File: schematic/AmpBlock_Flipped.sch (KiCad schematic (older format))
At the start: 12 parts, among them IC8 LTC6090CS8E#PBF

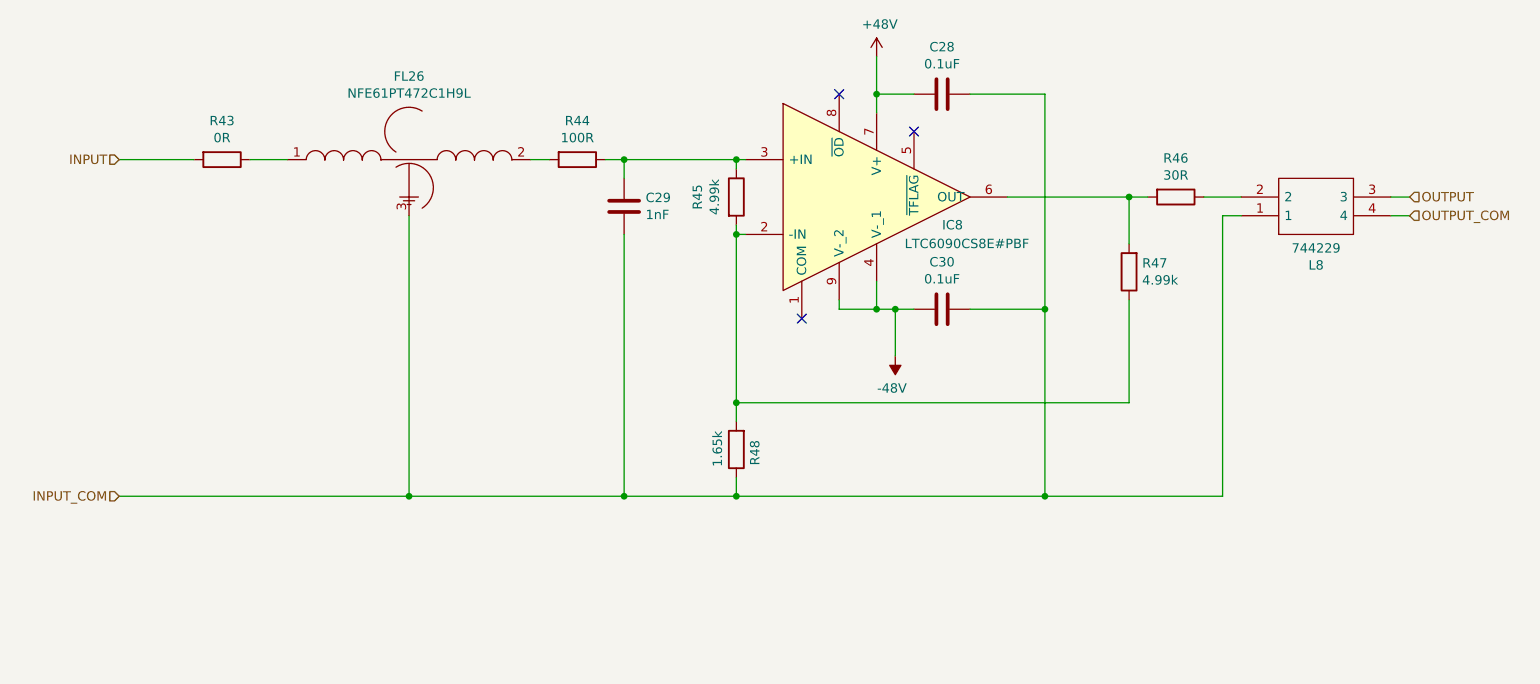
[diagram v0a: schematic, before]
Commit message: Updating with recent changes as layout work starts
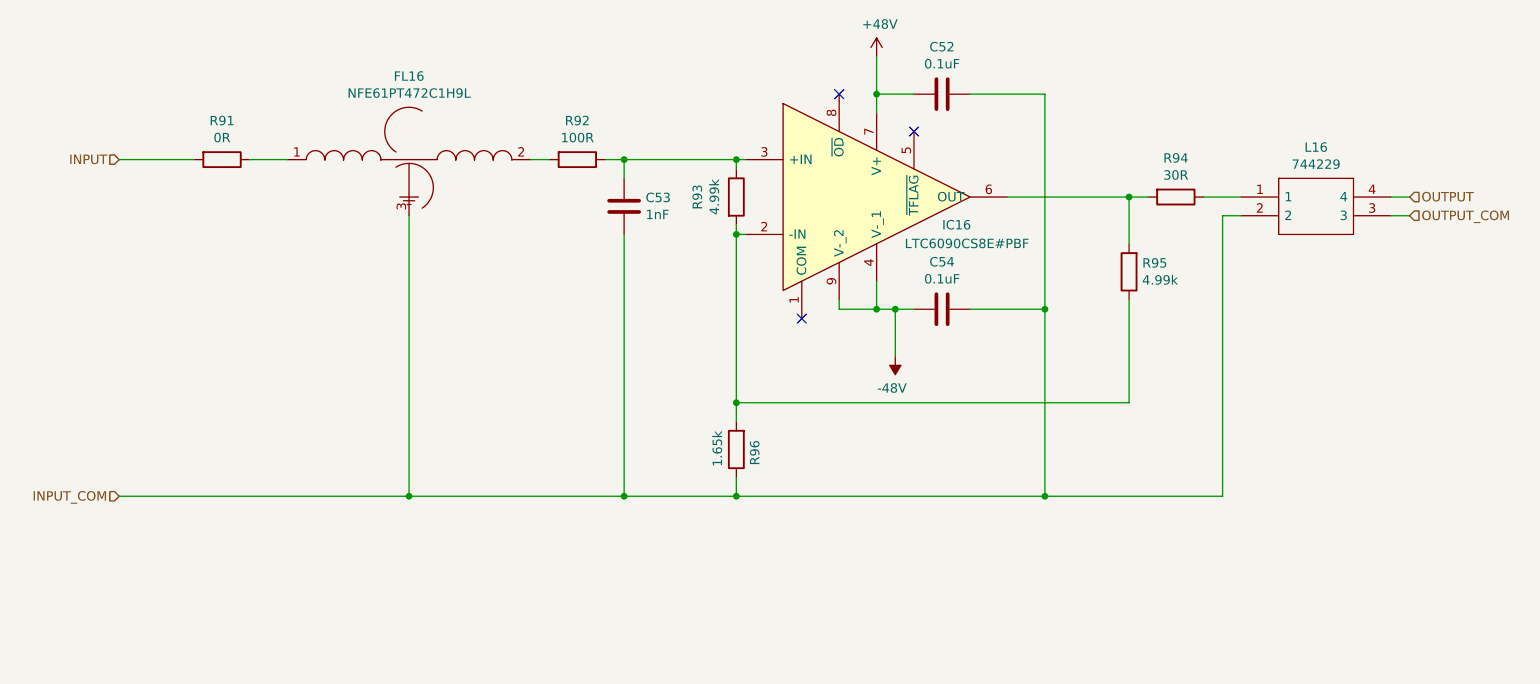
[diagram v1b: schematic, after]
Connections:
- net INPUT_COM: now also L8.2; no longer L8.1
- net OUTPUT: now also L8.4; no longer L8.3
- net OUTPUT_COM: now also L8.3; no longer L8.4
- net at R46.1: now also L8.1; no longer L8.2
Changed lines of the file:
@@
 $Descr A4 11693 8268
 encoding utf-8
-Sheet 26 33
+Sheet 17 33
 Title "Amplifier block"
 Date ""
@@
 AR Path="/5CAE2EB0/5C968DBB" Ref="R188"  Part="1"
 AR Path="/5C968DBB" Ref="R?"  Part="1"
-F 0 "R?" V 3743 3400 50  0000 C CNN
+F 0 "R92" V 3743 3400 50  0000 C CNN
 F 1 "100R" V 3834 3400 50  0000 C CNN
 F 2 "Resistor_SMD:R_0603_1608Metric" V 3880 3400 50  0001 C CNN
@@
 AR Path="/5CAE2EB0/5C969C02" Ref="R192"  Part="1"
 AR Path="/5C969C02" Ref="R?"  Part="1"
-F 0 "R?" V 4700 4900 50  0000 L CNN
+F 0 "R96" V 4700 4900 50  0000 L CNN
 F 1 "1.65k" V 4900 4850 50  0000 L CNN
 F 2 "Resistor_SMD:R_0603_1608Metric" V 4730 4950 50  0001 C CNN
@@
 AR Path="/5CAE2EB0/5C96A29C" Ref="R191"  Part="1"
 AR Path="/5C96A29C" Ref="R?"  Part="1"
-F 0 "R?" H 6830 3954 50  0000 R CNN
+F 0 "R95" H 6830 3954 50  0000 R CNN
 F 1 "4.99k" H 6830 4045 50  0000 R CNN
 F 2 "Resistor_SMD:R_0603_1608Metric" V 6830 4000 50  0001 C CNN
@@
 AR Path="/5CAE2EB0/5C96A628" Ref="C101"  Part="1"
 AR Path="/5C96A628" Ref="C?"  Part="1"
-F 0 "C?" H 4315 3696 50  0000 L CNN
+F 0 "C53" H 4315 3696 50  0000 L CNN
 F 1 "1nF" H 4315 3605 50  0000 L CNN
 F 2 "Capacitor_SMD:C_0603_1608Metric" H 4238 3500 50  0001 C CNN
@@
 AR Path="/5CAE2EB0/5C96EFD0" Ref="#PWR073"  Part="1"
 AR Path="/5C96EFD0" Ref="#PWR?"  Part="1"
-F 0 "#PWR?" H 5550 2700 50  0001 C CNN
+F 0 "#PWR073" H 5550 2700 50  0001 C CNN
 F 1 "+48V" H 5567 3023 50  0000 C CNN
 F 2 "" H 5550 2850 50  0001 C CNN
@@
 AR Path="/5CAE2EB0/5C96F7F1" Ref="#PWR074"  Part="1"
 AR Path="/5C96F7F1" Ref="#PWR?"  Part="1"
-F 0 "#PWR?" H 5650 4300 50  0001 C CNN
+F 0 "#PWR074" H 5650 4300 50  0001 C CNN
 F 1 "-48V" H 5668 4623 50  0000 C CNN
 F 2 "" H 5650 4450 50  0001 C CNN
@@
 AR Path="/5CAE2EB0/5C96FD85" Ref="C100"  Part="1"
 AR Path="/5C96FD85" Ref="C?"  Part="1"
-F 0 "C?" V 5648 3050 50  0000 C CNN
+F 0 "C52" V 5648 3050 50  0000 C CNN
 F 1 "0.1uF" V 5739 3050 50  0000 C CNN
 F 2 "Capacitor_SMD:C_0603_1608Metric" H 5938 2900 50  0001 C CNN
@@
 AR Path="/5CAE2EB0/5C97026D" Ref="C102"  Part="1"
 AR Path="/5C97026D" Ref="C?"  Part="1"
-F 0 "C?" V 5648 4200 50  0000 C CNN
+F 0 "C54" V 5648 4200 50  0000 C CNN
 F 1 "0.1uF" V 5739 4200 50  0000 C CNN
 F 2 "Capacitor_SMD:C_0603_1608Metric" H 5938 4050 50  0001 C CNN
@@
 AR Path="/5CAE2E6A/5E7F6ABF" Ref="FL31"  Part="1"
 AR Path="/5CAE2EB0/5E7F6ABF" Ref="FL32"  Part="1"
-F 0 "FL?" H 3050 3845 50  0000 C CNN
+F 0 "FL16" H 3050 3845 50  0000 C CNN
 F 1 "NFE61PT472C1H9L" H 3050 3754 50  0000 C CNN
 F 2 "ARTIQAmp:NFE61" H 3400 3650 50  0001 L CNN
@@
 AR Path="/5CAE2EB0/5F650121" Ref="R187"  Part="1"
 AR Path="/5F650121" Ref="R?"  Part="1"
-F 0 "R?" V 1843 3400 50  0000 C CNN
+F 0 "R91" V 1843 3400 50  0000 C CNN
 F 1 "0R" V 1934 3400 50  0000 C CNN
 F 2 "Resistor_SMD:R_0603_1608Metric" V 1980 3400 50  0001 C CNN
@@
 AR Path="/5CAE2EB0/5F6588CE" Ref="R189"  Part="1"
 AR Path="/5F6588CE" Ref="R?"  Part="1"
-F 0 "R?" V 4593 3600 50  0000 C CNN
+F 0 "R93" V 4593 3600 50  0000 C CNN
 F 1 "4.99k" V 4684 3600 50  0000 C CNN
 F 2 "Resistor_SMD:R_0603_1608Metric" V 4730 3600 50  0001 C CNN
@@
 AR Path="/5CAE2EB0/5F678EAA" Ref="R190"  Part="1"
 AR Path="/5F678EAA" Ref="R?"  Part="1"
-F 0 "R?" V 6943 3600 50  0000 C CNN
+F 0 "R94" V 6943 3600 50  0000 C CNN
 F 1 "30R" V 7034 3600 50  0000 C CNN
 F 2 "Resistor_SMD:R_0603_1608Metric" V 7080 3600 50  0001 C CNN
@@
 L ARTIQAmp:744229 L8
 U 1 1 5F68D18B
-P 7500 3700
+P 7500 3600
 AR Path="/5C968447/5F68D18B" Ref="L8"  Part="1"
 AR Path="/5C9C2F57/5F68D18B" Ref="L1"  Part="1"
@@
 AR Path="/5CAE2E6A/5F68D18B" Ref="L31"  Part="1"
 AR Path="/5CAE2EB0/5F68D18B" Ref="L32"  Part="1"
-F 0 "L?" H 7900 3965 50  0000 C CNN
-F 1 "744229" H 7900 3874 50  0000 C CNN
-F 2 "ARTIQAmp:WE-SL2" H 8150 3800 50  0001 L CNN
-F 3 "http://componentsearchengine.com/Datasheets/1/744229.pdf" H 8150 3700 50  0001 L CNN
-F 4 "SMD Common Mode Line Filter WE-SL5" H 8150 3600 50  0001 L CNN "Description"
-F 5 "Wurth Elektronik" H 8150 3200 50  0001 L CNN "Manufacturer_Name"
-F 6 "744229" H 8150 3100 50  0001 L CNN "Manufacturer_Part_Number"
-	1    7500 3700
-	1    0    0    1
+F 0 "L16" H 7900 3865 50  0000 C CNN
+F 1 "744229" H 7900 3774 50  0000 C CNN
+F 2 "ARTIQAmp:WE-SL2" H 8150 3700 50  0001 L CNN
+F 3 "http://componentsearchengine.com/Datasheets/1/744229.pdf" H 8150 3600 50  0001 L CNN
+F 4 "SMD Common Mode Line Filter WE-SL5" H 8150 3500 50  0001 L CNN "Description"
+F 5 "Wurth Elektronik" H 8150 3100 50  0001 L CNN "Manufacturer_Name"
+F 6 "744229" H 8150 3000 50  0001 L CNN "Manufacturer_Part_Number"
+	1    7500 3600
+	1    0    0    -1
 $EndComp
 $Comp
@@
 AR Path="/5CAE2E6A/5F68D7CC" Ref="IC31"  Part="1"
 AR Path="/5CAE2EB0/5F68D7CC" Ref="IC32"  Part="1"
-F 0 "IC?" H 5900 3450 50  0000 L CNN
+F 0 "IC16" H 5900 3450 50  0000 L CNN
 F 1 "LTC6090CS8E#PBF" H 5700 3350 50  0000 L CNN
 F 2 "ARTIQAmp:SOIC127P599X175-9N" H 5600 4200 50  0001 L CNN

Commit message: Complete initial layout and swap components around in schematic
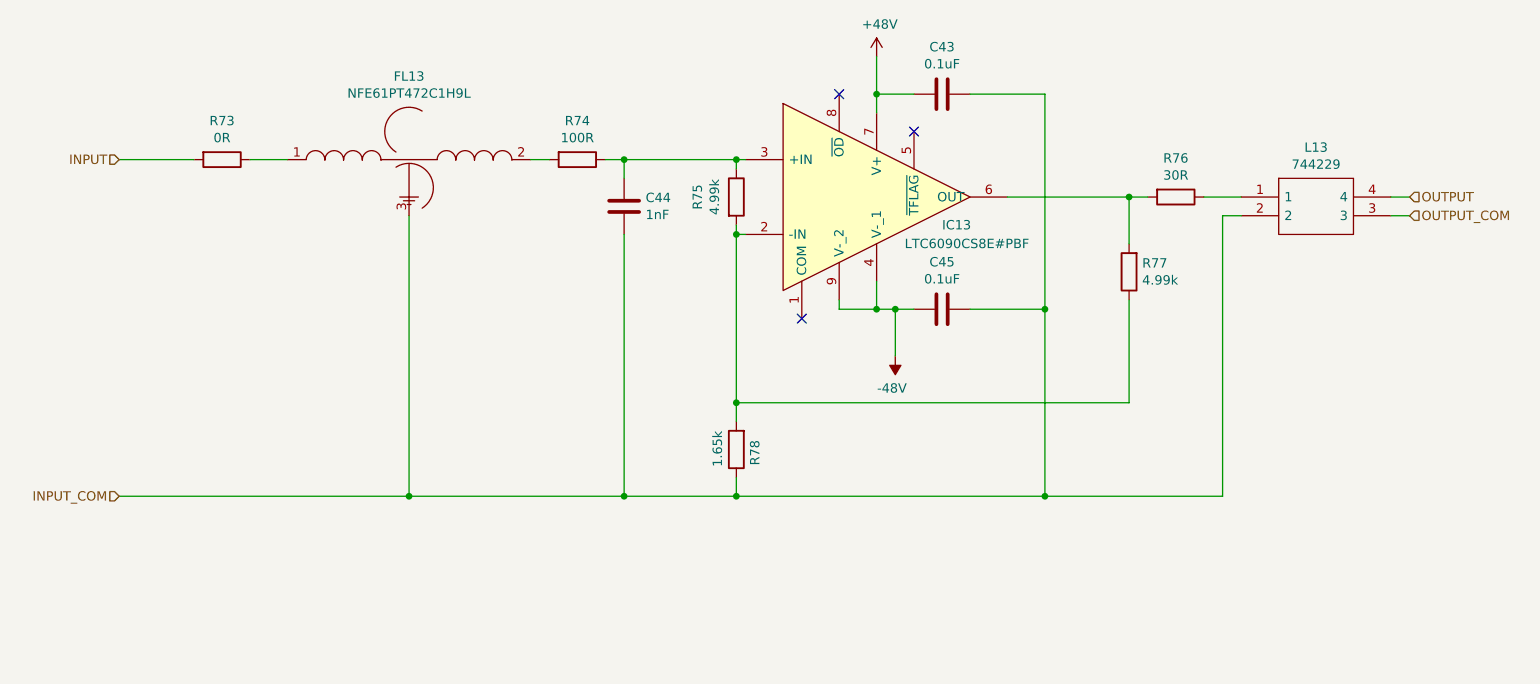
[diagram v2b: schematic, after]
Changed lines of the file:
@@
 $Descr A4 11693 8268
 encoding utf-8
-Sheet 17 33
+Sheet 14 33
 Title "Amplifier block"
 Date ""
@@
 AR Path="/5CAE2EB0/5C968DBB" Ref="R188"  Part="1"
 AR Path="/5C968DBB" Ref="R?"  Part="1"
-F 0 "R92" V 3743 3400 50  0000 C CNN
+F 0 "R74" V 3743 3400 50  0000 C CNN
 F 1 "100R" V 3834 3400 50  0000 C CNN
 F 2 "Resistor_SMD:R_0603_1608Metric" V 3880 3400 50  0001 C CNN
@@
 AR Path="/5CAE2EB0/5C969C02" Ref="R192"  Part="1"
 AR Path="/5C969C02" Ref="R?"  Part="1"
-F 0 "R96" V 4700 4900 50  0000 L CNN
+F 0 "R78" V 4700 4900 50  0000 L CNN
 F 1 "1.65k" V 4900 4850 50  0000 L CNN
 F 2 "Resistor_SMD:R_0603_1608Metric" V 4730 4950 50  0001 C CNN
@@
 AR Path="/5CAE2EB0/5C96A29C" Ref="R191"  Part="1"
 AR Path="/5C96A29C" Ref="R?"  Part="1"
-F 0 "R95" H 6830 3954 50  0000 R CNN
+F 0 "R77" H 6830 3954 50  0000 R CNN
 F 1 "4.99k" H 6830 4045 50  0000 R CNN
 F 2 "Resistor_SMD:R_0603_1608Metric" V 6830 4000 50  0001 C CNN
@@
 AR Path="/5CAE2EB0/5C96A628" Ref="C101"  Part="1"
 AR Path="/5C96A628" Ref="C?"  Part="1"
-F 0 "C53" H 4315 3696 50  0000 L CNN
+F 0 "C44" H 4315 3696 50  0000 L CNN
 F 1 "1nF" H 4315 3605 50  0000 L CNN
 F 2 "Capacitor_SMD:C_0603_1608Metric" H 4238 3500 50  0001 C CNN
@@
 AR Path="/5CAE2EB0/5C96EFD0" Ref="#PWR073"  Part="1"
 AR Path="/5C96EFD0" Ref="#PWR?"  Part="1"
-F 0 "#PWR073" H 5550 2700 50  0001 C CNN
+F 0 "#PWR057" H 5550 2700 50  0001 C CNN
 F 1 "+48V" H 5567 3023 50  0000 C CNN
 F 2 "" H 5550 2850 50  0001 C CNN
@@
 AR Path="/5CAE2EB0/5C96F7F1" Ref="#PWR074"  Part="1"
 AR Path="/5C96F7F1" Ref="#PWR?"  Part="1"
-F 0 "#PWR074" H 5650 4300 50  0001 C CNN
+F 0 "#PWR058" H 5650 4300 50  0001 C CNN
 F 1 "-48V" H 5668 4623 50  0000 C CNN
 F 2 "" H 5650 4450 50  0001 C CNN
@@
 AR Path="/5CAE2EB0/5C96FD85" Ref="C100"  Part="1"
 AR Path="/5C96FD85" Ref="C?"  Part="1"
-F 0 "C52" V 5648 3050 50  0000 C CNN
+F 0 "C43" V 5648 3050 50  0000 C CNN
 F 1 "0.1uF" V 5739 3050 50  0000 C CNN
 F 2 "Capacitor_SMD:C_0603_1608Metric" H 5938 2900 50  0001 C CNN
@@
 AR Path="/5CAE2EB0/5C97026D" Ref="C102"  Part="1"
 AR Path="/5C97026D" Ref="C?"  Part="1"
-F 0 "C54" V 5648 4200 50  0000 C CNN
+F 0 "C45" V 5648 4200 50  0000 C CNN
 F 1 "0.1uF" V 5739 4200 50  0000 C CNN
 F 2 "Capacitor_SMD:C_0603_1608Metric" H 5938 4050 50  0001 C CNN
@@
 AR Path="/5CAE2E6A/5E7F6ABF" Ref="FL31"  Part="1"
 AR Path="/5CAE2EB0/5E7F6ABF" Ref="FL32"  Part="1"
-F 0 "FL16" H 3050 3845 50  0000 C CNN
+F 0 "FL13" H 3050 3845 50  0000 C CNN
 F 1 "NFE61PT472C1H9L" H 3050 3754 50  0000 C CNN
 F 2 "ARTIQAmp:NFE61" H 3400 3650 50  0001 L CNN
@@
 AR Path="/5CAE2EB0/5F650121" Ref="R187"  Part="1"
 AR Path="/5F650121" Ref="R?"  Part="1"
-F 0 "R91" V 1843 3400 50  0000 C CNN
+F 0 "R73" V 1843 3400 50  0000 C CNN
 F 1 "0R" V 1934 3400 50  0000 C CNN
 F 2 "Resistor_SMD:R_0603_1608Metric" V 1980 3400 50  0001 C CNN
@@
 AR Path="/5CAE2EB0/5F6588CE" Ref="R189"  Part="1"
 AR Path="/5F6588CE" Ref="R?"  Part="1"
-F 0 "R93" V 4593 3600 50  0000 C CNN
+F 0 "R75" V 4593 3600 50  0000 C CNN
 F 1 "4.99k" V 4684 3600 50  0000 C CNN
 F 2 "Resistor_SMD:R_0603_1608Metric" V 4730 3600 50  0001 C CNN
@@
 AR Path="/5CAE2EB0/5F678EAA" Ref="R190"  Part="1"
 AR Path="/5F678EAA" Ref="R?"  Part="1"
-F 0 "R94" V 6943 3600 50  0000 C CNN
+F 0 "R76" V 6943 3600 50  0000 C CNN
 F 1 "30R" V 7034 3600 50  0000 C CNN
 F 2 "Resistor_SMD:R_0603_1608Metric" V 7080 3600 50  0001 C CNN
@@
 AR Path="/5CAE2E6A/5F68D18B" Ref="L31"  Part="1"
 AR Path="/5CAE2EB0/5F68D18B" Ref="L32"  Part="1"
-F 0 "L16" H 7900 3865 50  0000 C CNN
+F 0 "L13" H 7900 3865 50  0000 C CNN
 F 1 "744229" H 7900 3774 50  0000 C CNN
 F 2 "ARTIQAmp:WE-SL2" H 8150 3700 50  0001 L CNN
@@
 AR Path="/5CAE2E6A/5F68D7CC" Ref="IC31"  Part="1"
 AR Path="/5CAE2EB0/5F68D7CC" Ref="IC32"  Part="1"
-F 0 "IC16" H 5900 3450 50  0000 L CNN
+F 0 "IC13" H 5900 3450 50  0000 L CNN
 F 1 "LTC6090CS8E#PBF" H 5700 3350 50  0000 L CNN
 F 2 "ARTIQAmp:SOIC127P599X175-9N" H 5600 4200 50  0001 L CNN

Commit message: Board updates and starting to add more capacitors
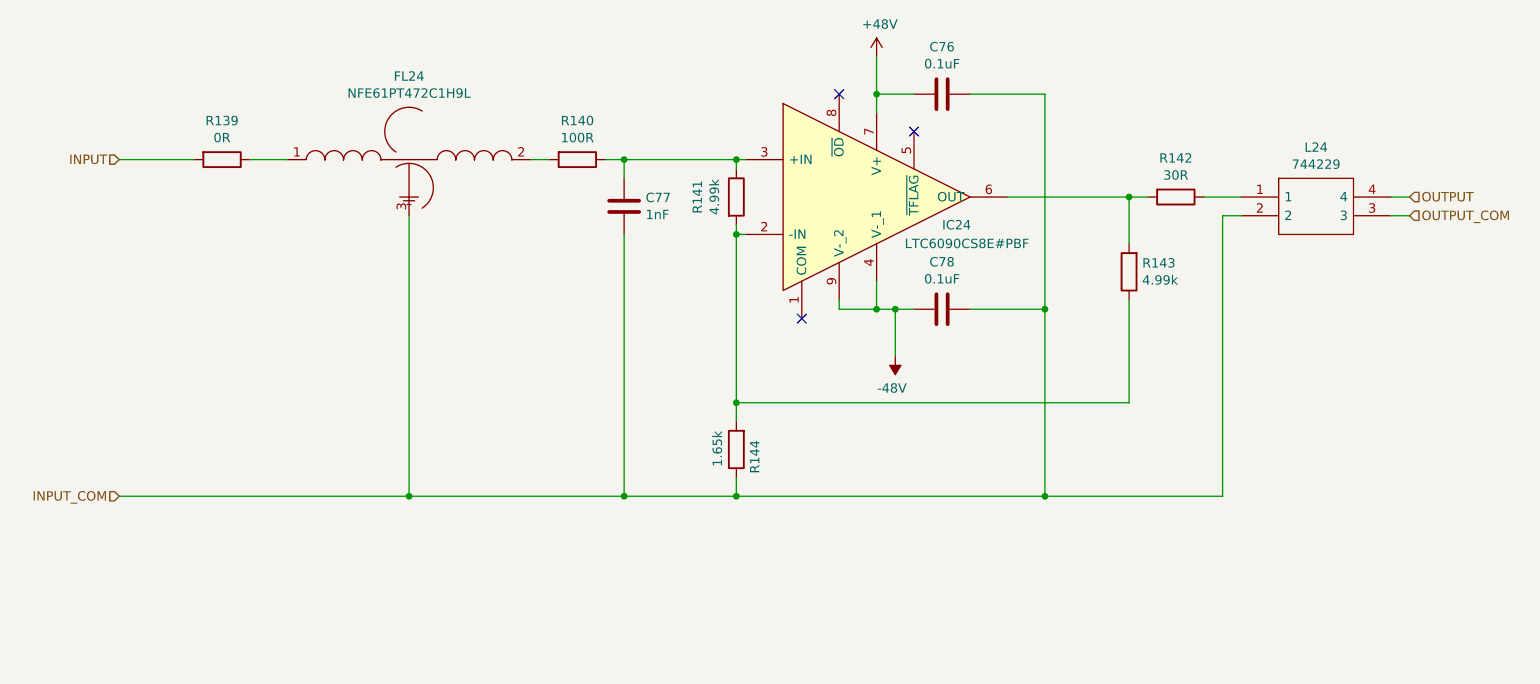
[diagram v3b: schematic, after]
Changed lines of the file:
@@
 $Descr A4 11693 8268
 encoding utf-8
-Sheet 14 33
+Sheet 25 33
 Title "Amplifier block"
 Date ""
@@
 AR Path="/5CAE2EB0/5C968DBB" Ref="R188"  Part="1"
 AR Path="/5C968DBB" Ref="R?"  Part="1"
-F 0 "R74" V 3743 3400 50  0000 C CNN
+F 0 "R140" V 3743 3400 50  0000 C CNN
 F 1 "100R" V 3834 3400 50  0000 C CNN
 F 2 "Resistor_SMD:R_0603_1608Metric" V 3880 3400 50  0001 C CNN
@@
 AR Path="/5CAE2EB0/5C969C02" Ref="R192"  Part="1"
 AR Path="/5C969C02" Ref="R?"  Part="1"
-F 0 "R78" V 4700 4900 50  0000 L CNN
+F 0 "R144" V 4700 4900 50  0000 L CNN
 F 1 "1.65k" V 4900 4850 50  0000 L CNN
 F 2 "Resistor_SMD:R_0603_1608Metric" V 4730 4950 50  0001 C CNN
@@
 AR Path="/5CAE2EB0/5C96A29C" Ref="R191"  Part="1"
 AR Path="/5C96A29C" Ref="R?"  Part="1"
-F 0 "R77" H 6830 3954 50  0000 R CNN
+F 0 "R143" H 6830 3954 50  0000 R CNN
 F 1 "4.99k" H 6830 4045 50  0000 R CNN
 F 2 "Resistor_SMD:R_0603_1608Metric" V 6830 4000 50  0001 C CNN
@@
 AR Path="/5CAE2EB0/5C96A628" Ref="C101"  Part="1"
 AR Path="/5C96A628" Ref="C?"  Part="1"
-F 0 "C44" H 4315 3696 50  0000 L CNN
+F 0 "C77" H 4315 3696 50  0000 L CNN
 F 1 "1nF" H 4315 3605 50  0000 L CNN
 F 2 "Capacitor_SMD:C_0603_1608Metric" H 4238 3500 50  0001 C CNN
@@
 AR Path="/5CAE2EB0/5C96FD85" Ref="C100"  Part="1"
 AR Path="/5C96FD85" Ref="C?"  Part="1"
-F 0 "C43" V 5648 3050 50  0000 C CNN
+F 0 "C76" V 5648 3050 50  0000 C CNN
 F 1 "0.1uF" V 5739 3050 50  0000 C CNN
 F 2 "Capacitor_SMD:C_0603_1608Metric" H 5938 2900 50  0001 C CNN
@@
 AR Path="/5CAE2EB0/5C97026D" Ref="C102"  Part="1"
 AR Path="/5C97026D" Ref="C?"  Part="1"
-F 0 "C45" V 5648 4200 50  0000 C CNN
+F 0 "C78" V 5648 4200 50  0000 C CNN
 F 1 "0.1uF" V 5739 4200 50  0000 C CNN
 F 2 "Capacitor_SMD:C_0603_1608Metric" H 5938 4050 50  0001 C CNN
@@
 AR Path="/5CAE2E6A/5E7F6ABF" Ref="FL31"  Part="1"
 AR Path="/5CAE2EB0/5E7F6ABF" Ref="FL32"  Part="1"
-F 0 "FL13" H 3050 3845 50  0000 C CNN
+F 0 "FL24" H 3050 3845 50  0000 C CNN
 F 1 "NFE61PT472C1H9L" H 3050 3754 50  0000 C CNN
 F 2 "ARTIQAmp:NFE61" H 3400 3650 50  0001 L CNN
@@
 AR Path="/5CAE2EB0/5F650121" Ref="R187"  Part="1"
 AR Path="/5F650121" Ref="R?"  Part="1"
-F 0 "R73" V 1843 3400 50  0000 C CNN
+F 0 "R139" V 1843 3400 50  0000 C CNN
 F 1 "0R" V 1934 3400 50  0000 C CNN
 F 2 "Resistor_SMD:R_0603_1608Metric" V 1980 3400 50  0001 C CNN
@@
 AR Path="/5CAE2EB0/5F6588CE" Ref="R189"  Part="1"
 AR Path="/5F6588CE" Ref="R?"  Part="1"
-F 0 "R75" V 4593 3600 50  0000 C CNN
+F 0 "R141" V 4593 3600 50  0000 C CNN
 F 1 "4.99k" V 4684 3600 50  0000 C CNN
 F 2 "Resistor_SMD:R_0603_1608Metric" V 4730 3600 50  0001 C CNN
@@
 AR Path="/5CAE2EB0/5F678EAA" Ref="R190"  Part="1"
 AR Path="/5F678EAA" Ref="R?"  Part="1"
-F 0 "R76" V 6943 3600 50  0000 C CNN
+F 0 "R142" V 6943 3600 50  0000 C CNN
 F 1 "30R" V 7034 3600 50  0000 C CNN
 F 2 "Resistor_SMD:R_0603_1608Metric" V 7080 3600 50  0001 C CNN
@@
 AR Path="/5CAE2E6A/5F68D18B" Ref="L31"  Part="1"
 AR Path="/5CAE2EB0/5F68D18B" Ref="L32"  Part="1"
-F 0 "L13" H 7900 3865 50  0000 C CNN
+F 0 "L24" H 7900 3865 50  0000 C CNN
 F 1 "744229" H 7900 3774 50  0000 C CNN
 F 2 "ARTIQAmp:WE-SL2" H 8150 3700 50  0001 L CNN
@@
 AR Path="/5CAE2E6A/5F68D7CC" Ref="IC31"  Part="1"
 AR Path="/5CAE2EB0/5F68D7CC" Ref="IC32"  Part="1"
-F 0 "IC13" H 5900 3450 50  0000 L CNN
+F 0 "IC24" H 5900 3450 50  0000 L CNN
 F 1 "LTC6090CS8E#PBF" H 5700 3350 50  0000 L CNN
 F 2 "ARTIQAmp:SOIC127P599X175-9N" H 5600 4200 50  0001 L CNN

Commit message: Many updates to layout; nearing final design
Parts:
- added R209, R210: 0R, Resistor_SMD:R_0603_1608Metric, symbol Device:R
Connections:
- net INPUT_COM: now also R209.2, R210.2
- new net GND: R209.1, R210.1
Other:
- note added: "Optional connections to panel ground"
